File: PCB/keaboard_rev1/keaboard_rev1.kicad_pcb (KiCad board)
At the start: 2 copper layers, 136.5 x 87.7 mm, 63 parts, among them K01 KEYSW, K02 KEYSW, K03 KEYSW, K04 KEYSW, K05 KEYSW, K06 KEYSW, K07 KEYSW, K08 KEYSW, K09 KEYSW, K10 KEYSW, K11 KEYSW, K12 KEYSW, K13 KEYSW, K14 KEYSW, K15 KEYSW, K16 KEYSW, K17 KEYSW, K18 KEYSW, K19 KEYSW, K20 KEYSW, K21 KEYSW, K22 KEYSW, K23 KEYSW, K24 KEYSW, K25 KEYSW, U1 ProMicro

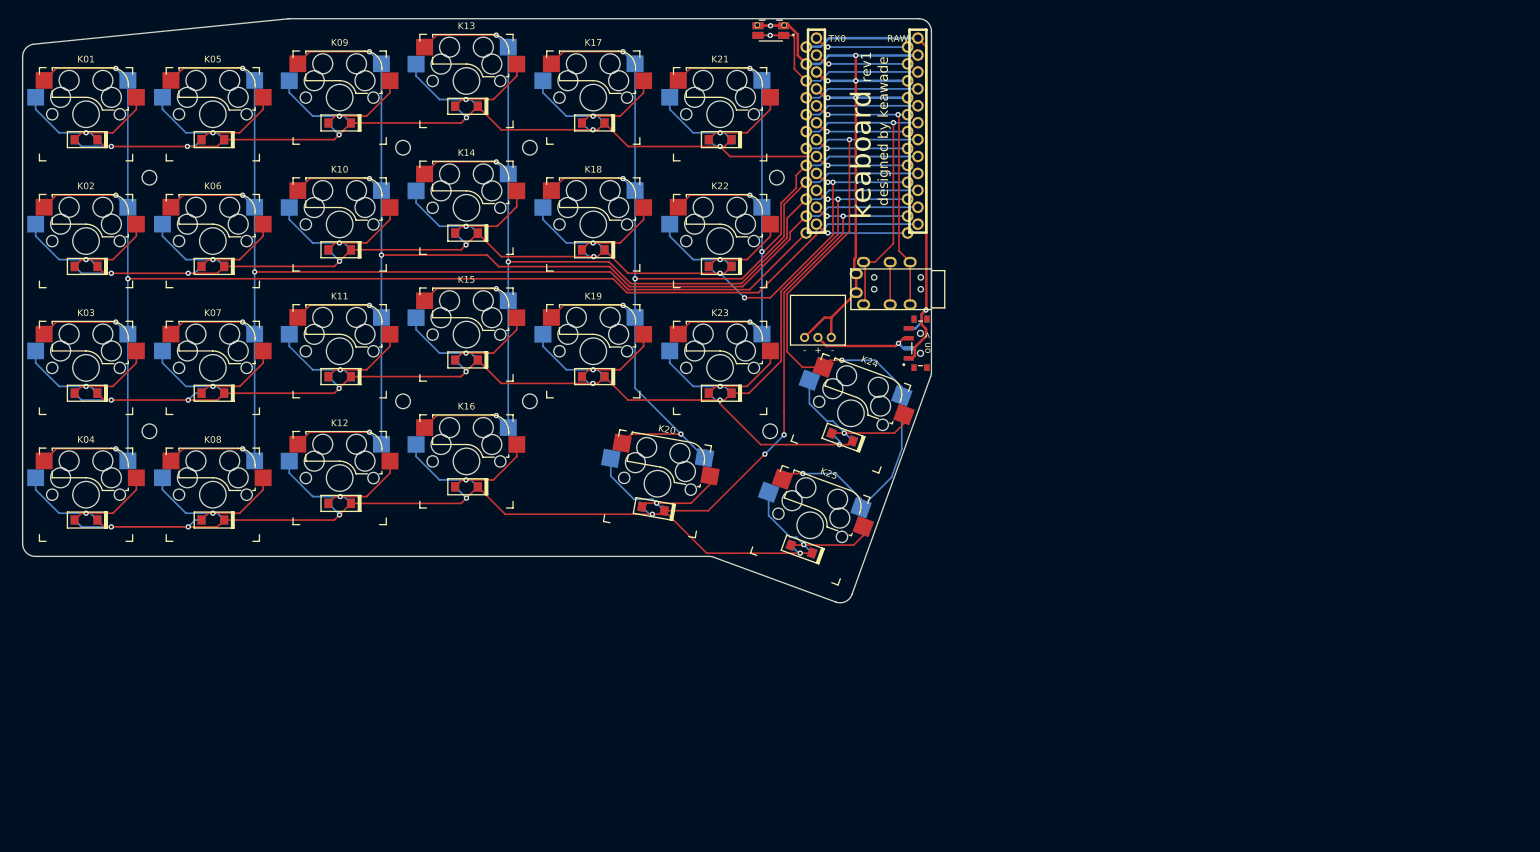
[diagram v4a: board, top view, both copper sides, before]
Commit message: Resize PCB to add more space around the edges to avoid breaking parts, update images, update gerber
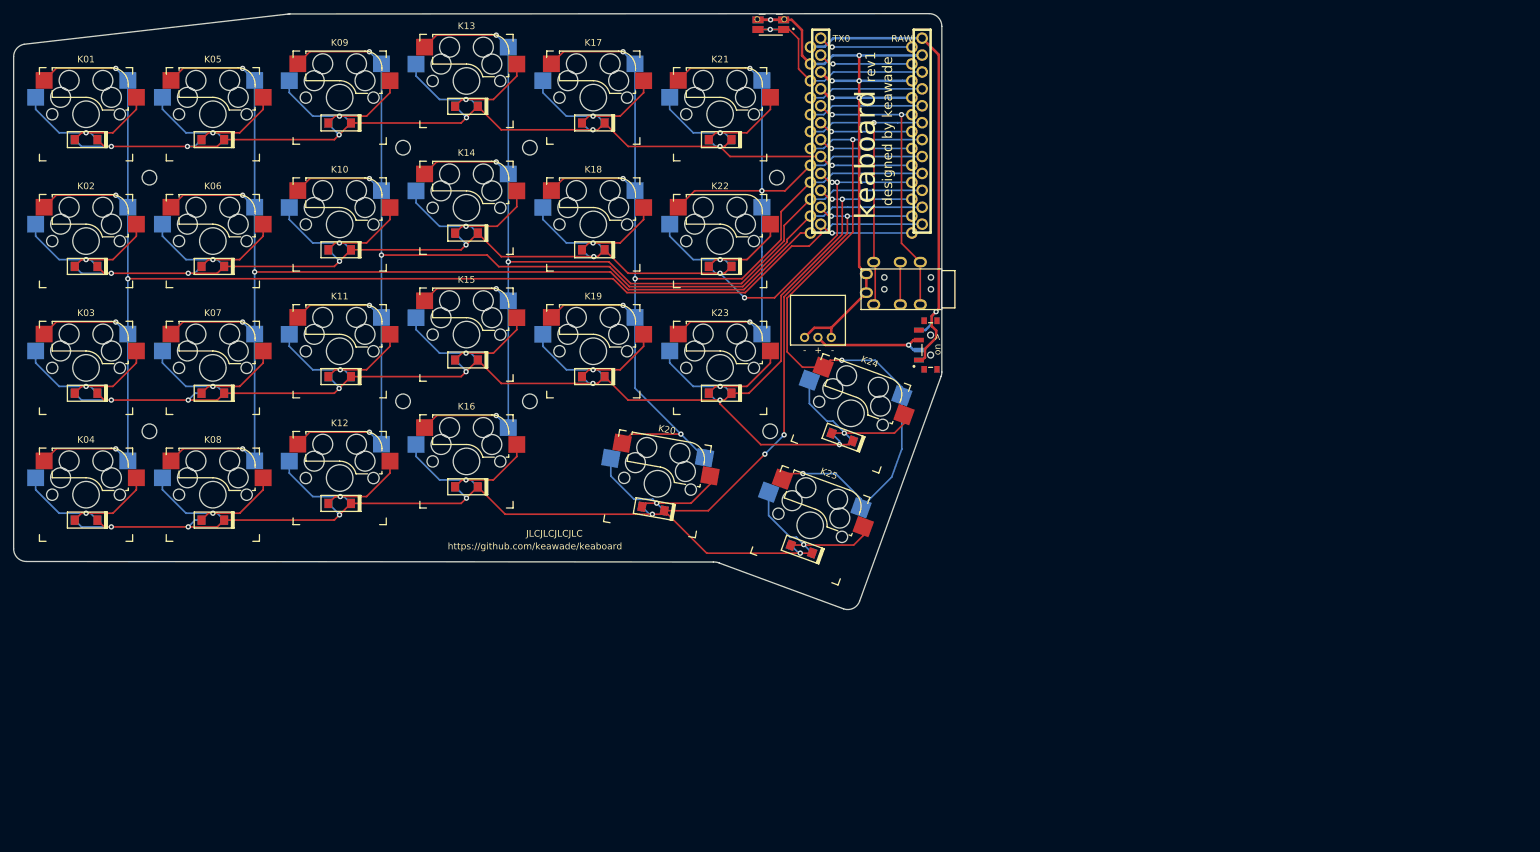
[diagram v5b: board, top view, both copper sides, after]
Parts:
- moved SW_PWR1 1.55 mm to (165.4, 76.7)
- moved TRRS1 1.52 mm to (167.0, 68.3)
- moved SW_RST1 0.89 mm to (141.4, 28.6)
- moved U1 0.63 mm to (156.5, 44.6)
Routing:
- net COL6: track 113.5 -> 106.0 mm, vias 4 -> 3
- net TRRS_TIP: track 47.7 -> 44.9 mm
- net GND: track 110.7 -> 112.3 mm
- net Net-(BAT1-Pad1): track 16.5 -> 17.8 mm
- net RAW: track 72.3 -> 73.2 mm
- net RESET: track 34.0 -> 34.9 mm
- net ROW1: track 148.8 -> 149.5 mm
- net ROW2: track 164.0 -> 164.7 mm
- net COL1: track 237.2 -> 237.8 mm
- net COL2: track 218.2 -> 218.8 mm
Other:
- board size 136.5 x 87.7 mm -> 139.4 x 89.5 mm
- board text added: "JLCJLCJLCJLC"
- board text added: "https://github.com/keawade/keaboard"

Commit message: Update schematic, update footprints, start updating layout
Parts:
- removed REF** (x8): MountingHole_2.2mm_M2, MountingHole:MountingHole_2.2mm_M2
- D01, D02, D03, D04, D05, D06, D07, D08, D09, D10, D11, D12, D13, D14, D15, D16, D17, D18, D19, D20, D21, D22, D23, D24, D25: moved to F.Cu
- moved D25 39.3 mm to (157.0, 145.1), turned to 250 degrees
- moved D24 38.3 mm to (163.5, 127.2), turned to 250 degrees
- moved D20 36.4 mm to (130.6, 137.0), turned to 260 degrees
- moved K25 34.7 mm to (151.4, 138.3)
- moved K20 33.7 mm to (124.0, 131.3)
- moved K24 33.7 mm to (158.0, 120.4)
- moved D04 32.8 mm to (48.3, 134.3), turned to 270 degrees
- moved D01 32.8 mm to (48.3, 77.1), turned to 270 degrees
- moved D08 32.8 mm to (67.3, 134.3), turned to 270 degrees
- moved D21 32.8 mm to (143.5, 77.1), turned to 270 degrees
- moved D02 32.8 mm to (48.3, 96.2), turned to 270 degrees
- moved D03 32.8 mm to (48.3, 115.2), turned to 270 degrees
- moved D05 32.8 mm to (67.3, 77.1), turned to 270 degrees
- moved D22 32.8 mm to (143.5, 96.2), turned to 270 degrees
- moved D23 32.8 mm to (143.5, 115.2), turned to 270 degrees
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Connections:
- TRRS1 pad R2: TRRS_SLEEVE -> VCC
- TRRS1 pad T: TRRS_TIP -> SOFT_SERIAL_PIN
- U1 pad 10: ROW3 -> ROW2
- U1 pad 11: ROW4 -> ROW3
- U1 pad 12: COL1 -> ROW4
- U1 pad 13: COL2 -> COL7
- U1 pad 14: COL3 -> COL6
- U1 pad 15: COL4 -> COL5
- U1 pad 16: COL5 -> COL4
- U1 pad 17: COL6 -> COL3
- U1 pad 18: COL7 -> COL2
- U1 pad 19: TRRS_TIP -> COL1
- U1 pad 20: Net-(U1-Pad20) -> SOFT_SERIAL_PIN
- U1 pad 21: Net-(U1-Pad21) -> VCC
- U1 pad 5: TRRS_SLEEVE -> Net-(U1-Pad5)
- U1 pad 8: ROW1 -> Net-(U1-Pad8)
- U1 pad 9: ROW2 -> ROW1
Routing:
- net COL1: track 237.8 -> 131.3 mm, vias 6 -> 4
- net COL2: track 218.8 -> 131.3 mm, vias 5 -> 4
- net COL3: track 201.7 -> 131.3 mm, vias 5 -> 4
- net COL7: track 109.0 -> 45.9 mm, vias 3 -> 2
- net ROW4: track 205.8 -> 147.5 mm, vias 10 -> 7
- net COL5: track 167.2 -> 112.2 mm, vias 5 -> 4
- net COL4: track 184.0 -> 131.3 mm, vias 5 -> 4
- net VCC: track 0.00 -> 51.9 mm
- net GND: track 112.3 -> 60.5 mm, vias 6 -> 3
- net TRRS_TIP: track 44.9 -> 0.00 mm, vias 1 -> 0
- net TRRS_SLEEVE: track 44.0 -> 0.00 mm, vias 2 -> 0
- net ROW3: track 196.7 -> 157.2 mm, vias 9 -> 8
- net ROW2: track 164.7 -> 129.7 mm, vias 9 -> 7
- net SOFT_SERIAL_PIN: track 0.00 -> 24.5 mm
- net ROW1: track 149.5 -> 129.8 mm
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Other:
- board outline removed
- board text removed: "+"
- board text removed: "-"
- board text removed: "on >"

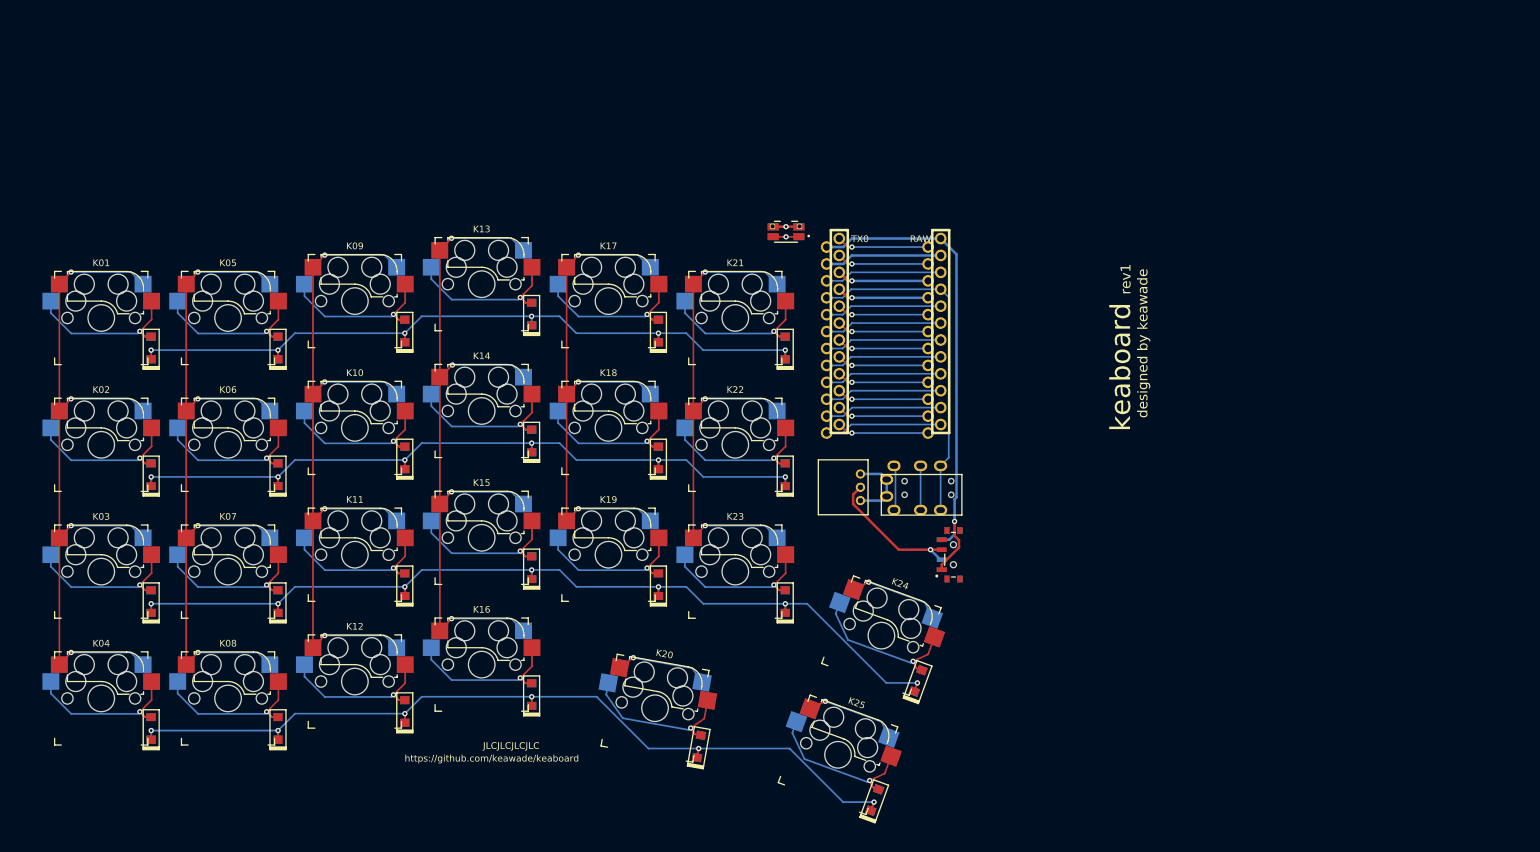
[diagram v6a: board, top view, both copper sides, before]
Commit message: Update cases, update edge cuts on main pcb, start routing traces to controller
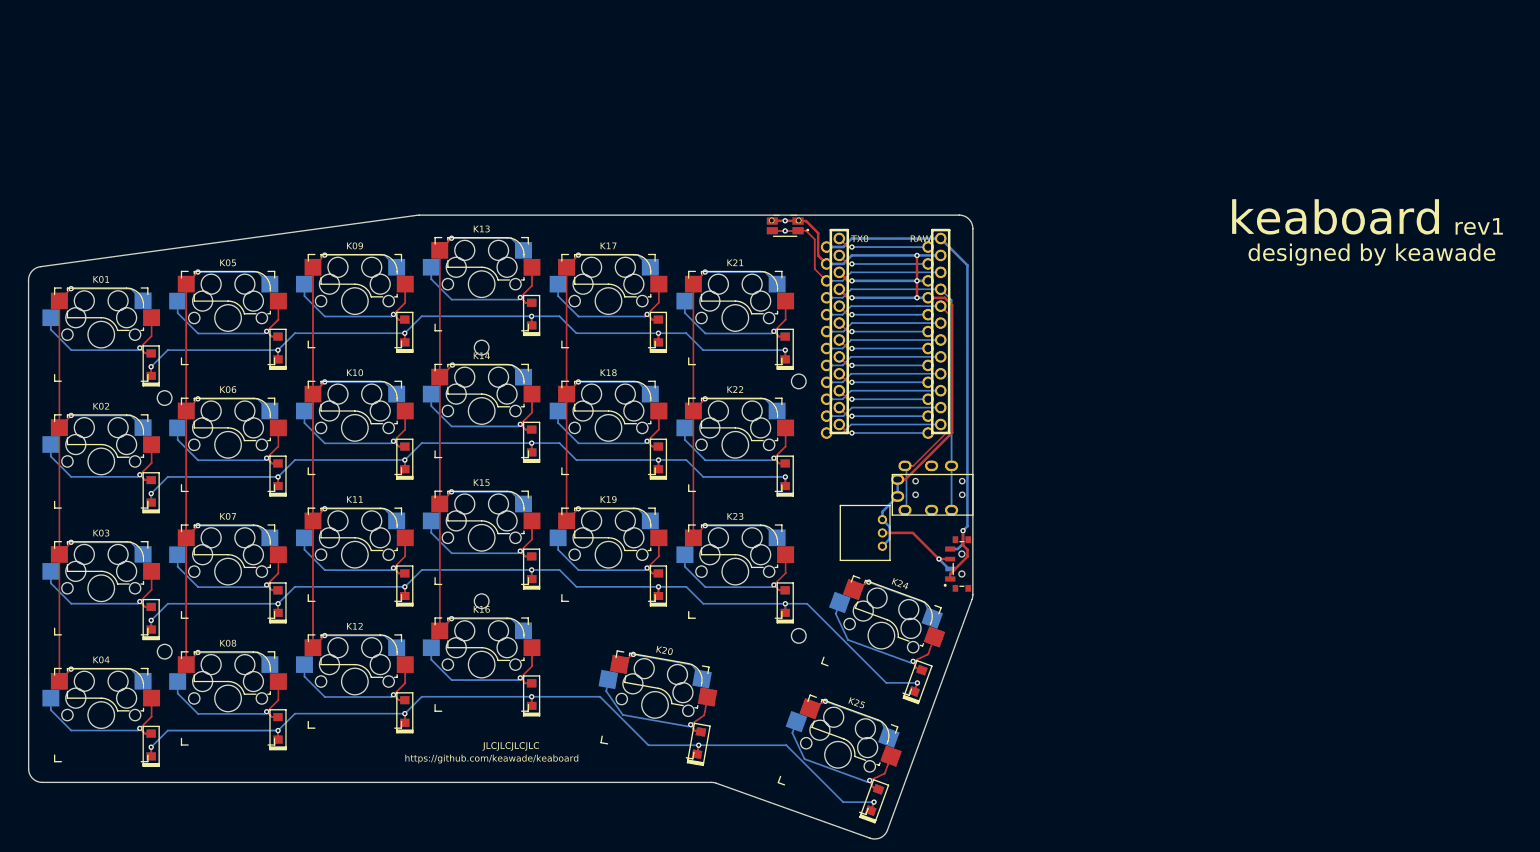
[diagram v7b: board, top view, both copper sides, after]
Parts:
- added REF**: MountingHole_2.2mm_M2, MountingHole:MountingHole_2.2mm_M2, F.Cu at (145.6, 82.2)
- added REF**: MountingHole_2.2mm_M2, MountingHole:MountingHole_2.2mm_M2, F.Cu at (145.6, 120.4)
- added REF**: MountingHole_2.2mm_M2, MountingHole:MountingHole_2.2mm_M2, F.Cu at (97.9, 77.1)
- added REF**: MountingHole_2.2mm_M2, MountingHole:MountingHole_2.2mm_M2, F.Cu at (97.9, 115.2)
- added REF**: MountingHole_2.2mm_M2, MountingHole:MountingHole_2.2mm_M2, F.Cu at (50.3, 122.8)
- added REF**: MountingHole_2.2mm_M2, MountingHole:MountingHole_2.2mm_M2, F.Cu at (50.3, 84.7)
- moved BAT1 7.61 mm to (158.1, 106.9)
- moved D01 2.50 mm to (48.3, 79.6)
- moved D02 2.50 mm to (48.3, 98.7)
- moved D03 2.50 mm to (48.3, 117.7)
- moved D04 2.50 mm to (48.3, 136.8)
- moved K01 2.50 mm to (40.8, 75.1)
- moved K02 2.50 mm to (40.8, 94.2)
- moved K03 2.50 mm to (40.8, 113.2)
- moved K04 2.50 mm to (40.8, 132.3)
- moved SW_PWR1 1.89 mm to (170.1, 109.6)
- moved TRRS1 1.65 mm to (171.7, 98.9)
- moved SW_RST1 0.90 mm to (143.5, 58.8)
- moved D20 0.50 mm to (130.6, 136.5)
- moved K20 0.50 mm to (124.0, 130.8)
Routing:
- net GND: track 60.5 -> 111.0 mm, vias 3 -> 6
- net SOFT_SERIAL_PIN: track 24.5 -> 52.5 mm
- net RESET: track 25.4 -> 35.5 mm
- net Net-(BAT1-Pad1): track 21.4 -> 14.1 mm
- net Net-(TRRS1-PadR1): track 6.65 -> 0.00 mm
- net RAW: track 74.1 -> 76.3 mm
- net ROW4: track 147.5 -> 148.6 mm
- net ROW3: track 157.2 -> 158.3 mm
- net ROW2: track 129.7 -> 130.8 mm
- net ROW1: track 129.8 -> 130.8 mm
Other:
- board outline added: 141.9 x 93.7 mm

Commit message: Route traces, add labels
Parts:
- moved BAT1 0.76 mm to (157.4, 106.9)
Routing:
- net COL1: track 131.3 -> 247.3 mm
- net COL2: track 131.3 -> 219.5 mm
- net COL3: track 131.3 -> 214.3 mm
- net COL4: track 131.3 -> 191.4 mm
- net ROW4: track 148.6 -> 207.2 mm
- net COL7: track 45.9 -> 94.0 mm
- net ROW3: track 158.3 -> 192.5 mm
- net COL5: track 112.2 -> 137.1 mm
- net COL6: track 98.1 -> 120.2 mm
- net ROW2: track 130.8 -> 148.5 mm
- net ROW1: track 130.8 -> 140.4 mm
- net Net-(BAT1-Pad1): track 14.1 -> 14.9 mm
